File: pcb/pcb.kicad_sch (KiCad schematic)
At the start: 23 parts

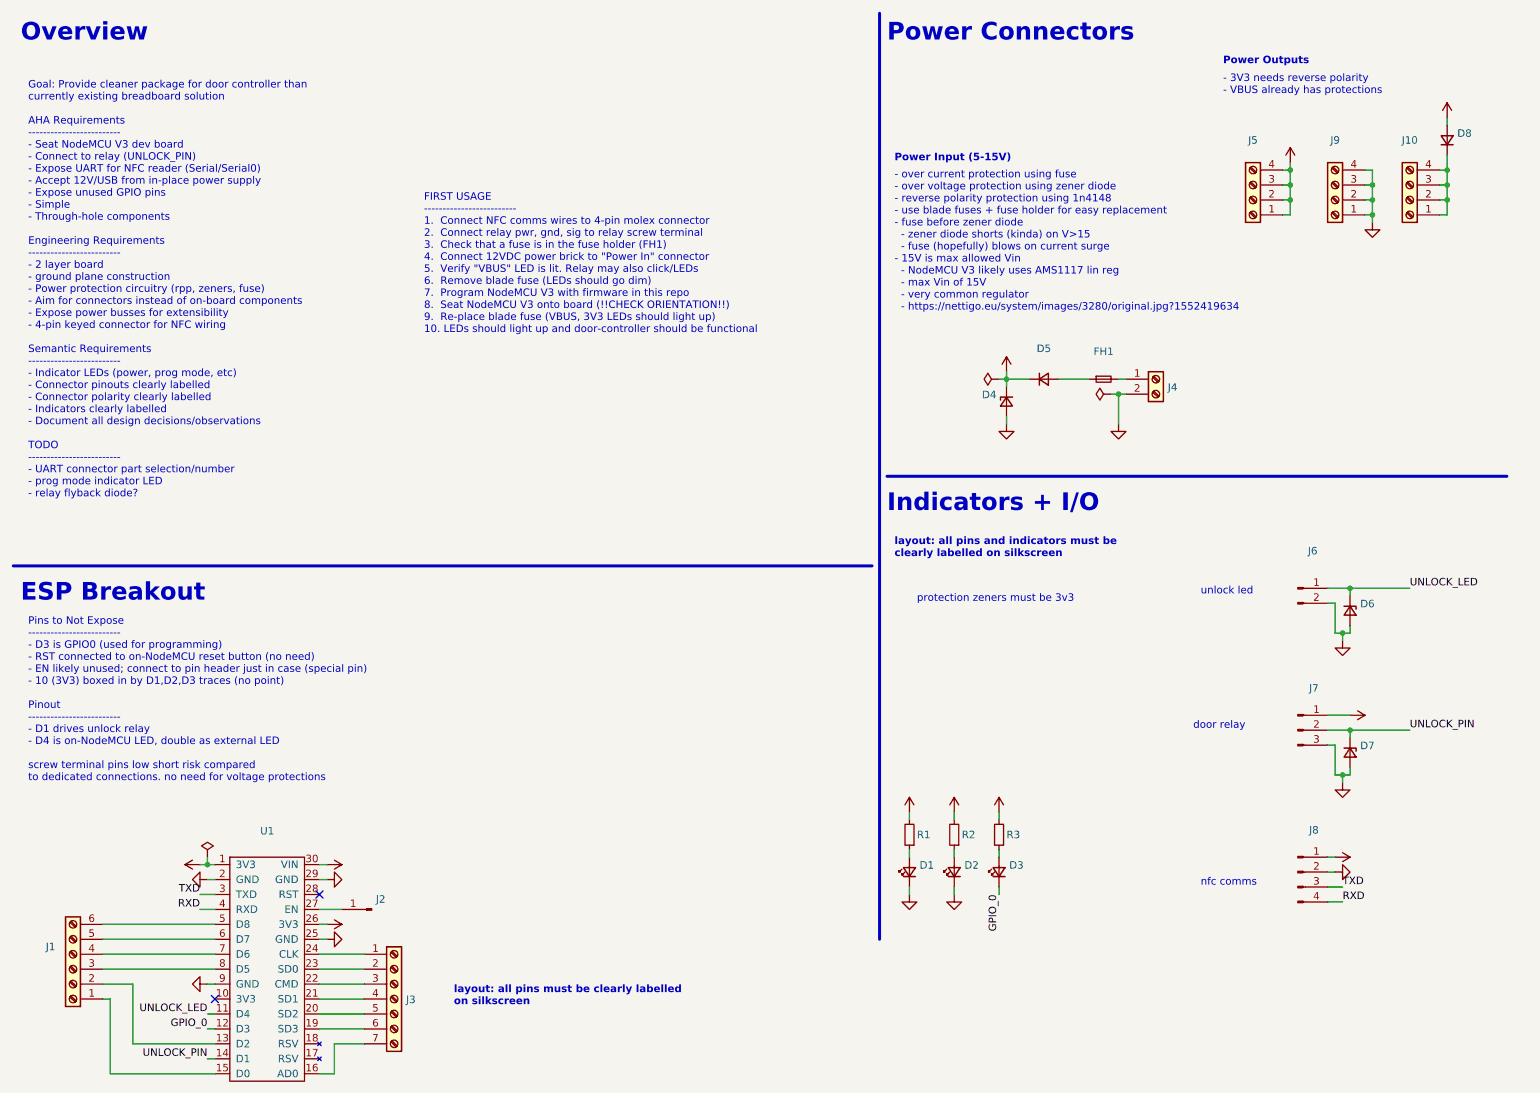
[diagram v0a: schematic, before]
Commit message: Update schematic with part numbers for BOM
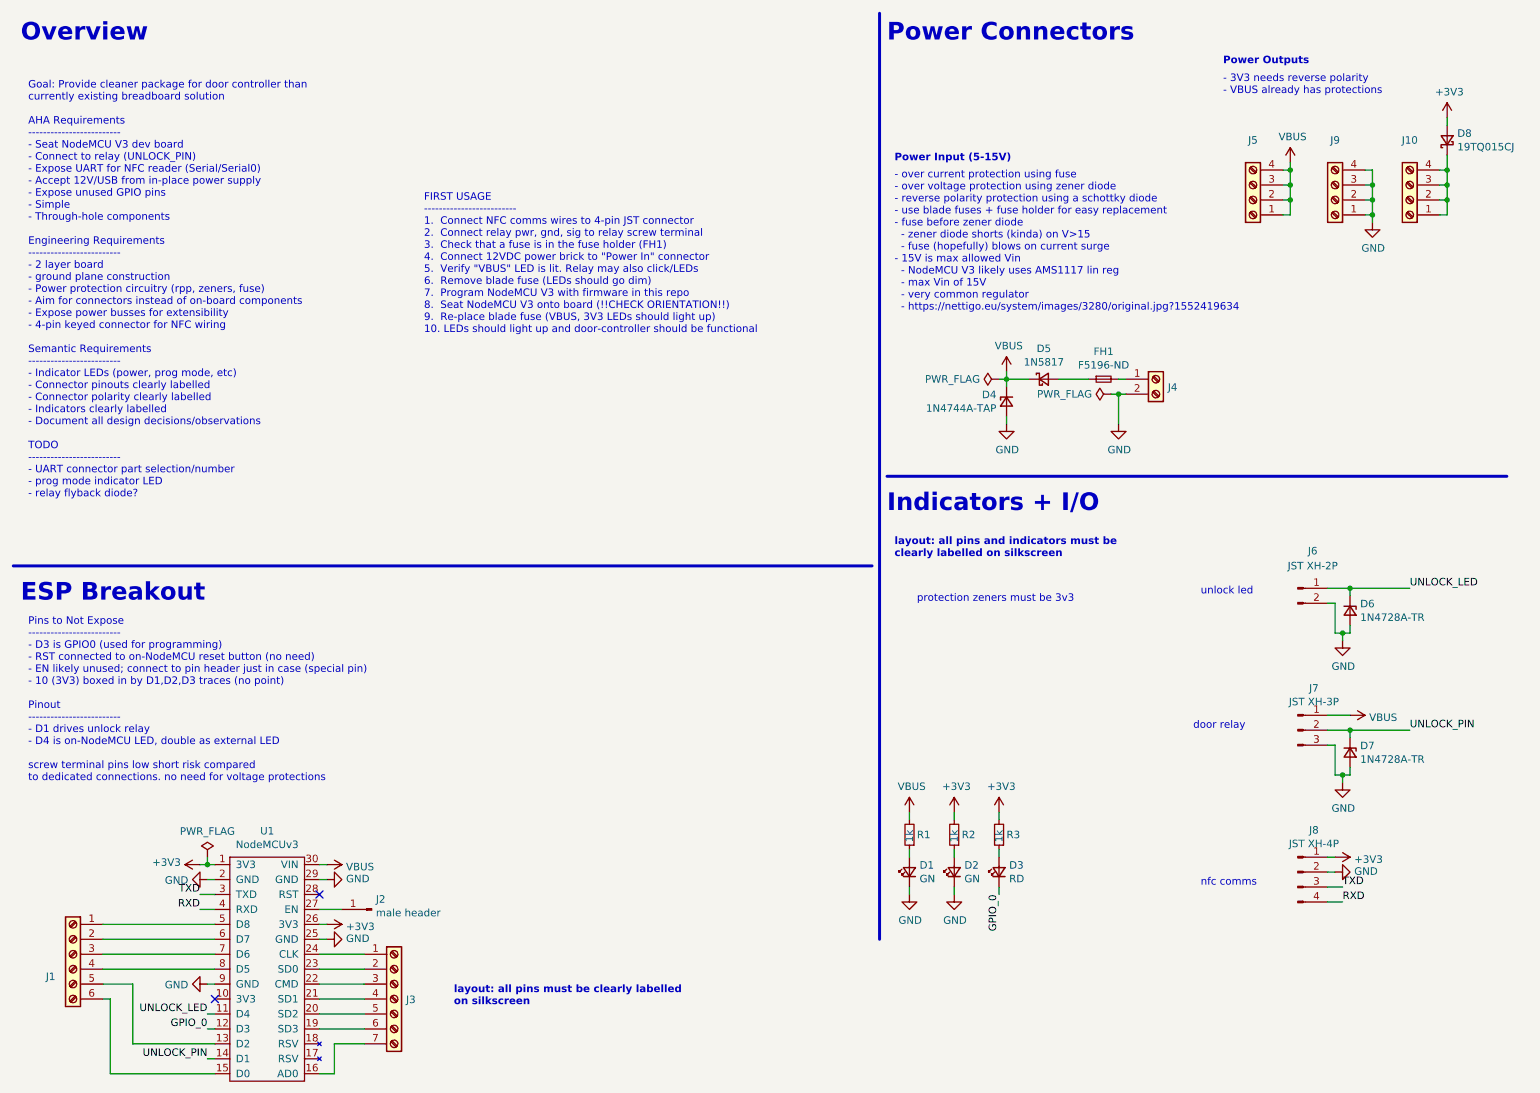
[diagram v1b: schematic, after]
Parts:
- D1, D2: value (none) -> GN; footprint (none) -> LED_THT:LED_D5.0mm; Digi-Key (none) -> 160-1130-ND; PartNo (none) -> LTL-4233
- D3: value (none) -> RD; footprint (none) -> LED_THT:LED_D5.0mm; Digi-Key (none) -> 160-1964-ND; PartNo (none) -> LTL-4263
- D4: value (none) -> 1N4744A-TAP; footprint (none) -> Diode_THT:D_DO-41_SOD81_P10.16mm_Horizontal; Digi-Key (none) -> 1N4744A-TAPGICT-ND; PartNo (none) -> 1N4744A-TAP
- D5: value (none) -> 1N5817; footprint (none) -> Diode_THT:D_DO-41_SOD81_P10.16mm_Horizontal; symbol Device:D_Small -> Device:D_Schottky_Small; Digi-Key (none) -> 1N5817-E3/54GICT-ND; PartNo (none) -> 1N5817-E3/54
- D6, D7: value (none) -> 1N4728A-TR; footprint (none) -> Diode_THT:D_DO-41_SOD81_P10.16mm_Horizontal; Digi-Key (none) -> 1N4728AVSCT-ND; PartNo (none) -> 1N4728A-TR
- D8: value (none) -> 19TQ015CJ; footprint (none) -> Package_TO_SOT_THT:TO-220-2_Vertical; symbol Device:D_Small -> Device:D_Schottky_Small; Digi-Key (none) -> 1655-1005-ND; PartNo (none) -> 19TQ015CJ
- FH1: value (none) -> F5196-ND; footprint (none) -> project:Blade Fuse Holder; Digi-Key (none) -> F5196-ND; PartNo (none) -> 178.6164.0002
- J1: value (none) -> Screw_Terminal_01x06; footprint (none) -> TerminalBlock_Phoenix:TerminalBlock_Phoenix_MPT-0,5-6-2.54_1x06_P2.54mm_Horizontal; Digi-Key (none) -> 277-1277-ND; PartNo (none) -> 1725698
- J10, J5, J9: value (none) -> Screw_Terminal_01x04; footprint (none) -> TerminalBlock_Phoenix:TerminalBlock_Phoenix_MPT-0,5-4-2.54_1x04_P2.54mm_Horizontal; Digi-Key (none) -> 277-1275-ND; PartNo (none) -> 1725672
- J2: value (none) -> male header; footprint (none) -> Connector_PinHeader_2.54mm:PinHeader_1x01_P2.54mm_Vertical; Digi-Key (none) -> 3M156413-01-ND; PartNo (none) -> 951101-8622-AR
- J3: value (none) -> Screw_Terminal_01x07; footprint (none) -> TerminalBlock_Phoenix:TerminalBlock_Phoenix_MPT-0,5-7-2.54_1x07_P2.54mm_Horizontal; Digi-Key (none) -> 277-1278-ND; PartNo (none) -> 1725708
- J4: value (none) -> Screw_Terminal_01x02; footprint (none) -> TerminalBlock_Phoenix:TerminalBlock_Phoenix_MPT-0,5-2-2.54_1x02_P2.54mm_Horizontal; Digi-Key (none) -> 277-1273-ND; PartNo (none) -> 1725656
- J6: value (none) -> JST XH-2P; footprint (none) -> Connector_JST:JST_XH_B2B-XH-AM_1x02_P2.50mm_Vertical; Digi-Key (none) -> 455-2946-ND; PartNo (none) -> B2B-XH-A-GU
- J7: value (none) -> JST XH-3P; footprint (none) -> Connector_JST:JST_XH_B3B-XH-AM_1x03_P2.50mm_Vertical; Digi-Key (none) -> 455-2231-ND; PartNo (none) -> B3B-XH-AM(LF)(SN)
- J8: value (none) -> JST XH-4P; footprint (none) -> Connector_JST:JST_XH_B4B-XH-AM_1x04_P2.50mm_Vertical; Digi-Key (none) -> 455-2237-ND; PartNo (none) -> B4B-XH-AM(LF)(SN)
- R1, R2, R3: value (none) -> 1k; footprint (none) -> Resistor_THT:R_Axial_DIN0207_L6.3mm_D2.5mm_P10.16mm_Horizontal; Digi-Key (none) -> CF14JT1K00CT-ND; PartNo (none) -> CF14JT1K00
- U1: value (none) -> NodeMCUv3; footprint (none) -> project:NodeMCUv3
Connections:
- net at U1.13 (D2): now also J1.5 (Pin_5); no longer J1.2 (Pin_2)
- net at U1.15 (D0): now also J1.6 (Pin_6); no longer J1.1 (Pin_1)
- net at U1.5 (D8): now also J1.1 (Pin_1); no longer J1.6 (Pin_6)
- net at U1.6 (D7): now also J1.2 (Pin_2); no longer J1.5 (Pin_5)
- net at U1.7 (D6): now also J1.3 (Pin_3); no longer J1.4 (Pin_4)
- net at U1.8 (D5): now also J1.4 (Pin_4); no longer J1.3 (Pin_3)
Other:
- note added: "- over current protection using fuse - over voltage protection using zener diode - reverse polarity protection using a schottky diode - use blade fuses + fuse holder for easy replacement - fuse before zener diode - zener diode shorts (kinda) on V>15 - fuse (hopefully) blows on current surge - 15V is max allowed Vin - NodeMCU V3 likely uses AMS1117 lin reg - max Vin of 15V - very common regulator 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"
- note added: "FIRST USAGE ------------------------- 1. Connect NFC comms wires to 4-pin JST connector 2. Connect relay pwr, gnd, sig to relay screw terminal 3. Check that a fuse is in the fuse holder (FH1) 4. Connect 12VDC power brick to "Power In" connector 5. Verify "VBUS" LED is lit. Relay may also click/LEDs 6. Remove blade fuse (LEDs should go dim) 7. Program NodeMCU V3 with firmware in this repo 8. Seat 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"
- note removed: "- over current protection using fuse - over voltage protection using zener diode - reverse polarity protection using 1n4148 - use blade fuses + fuse holder for easy replacement - fuse before zener diode - zener diode shorts (kinda) on V>15 - fuse (hopefully) blows on current surge - 15V is max allowed Vin - NodeMCU V3 likely uses AMS1117 lin reg - max Vin of 15V - very common regulator - https://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"
- note removed: "FIRST USAGE ------------------------- 1. Connect NFC comms wires to 4-pin molex connector 2. Connect relay pwr, gnd, sig to relay screw terminal 3. Check that a fuse is in the fuse holder (FH1) 4. Connect 12VDC power brick to "Power In" connector 5. Verify "VBUS" LED is lit. Relay may also click/LEDs 6. Remove blade fuse (LEDs should go dim) 7. Program NodeMCU V3 with firmware in this repo 8. Sea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"
- moved on the sheet: J1

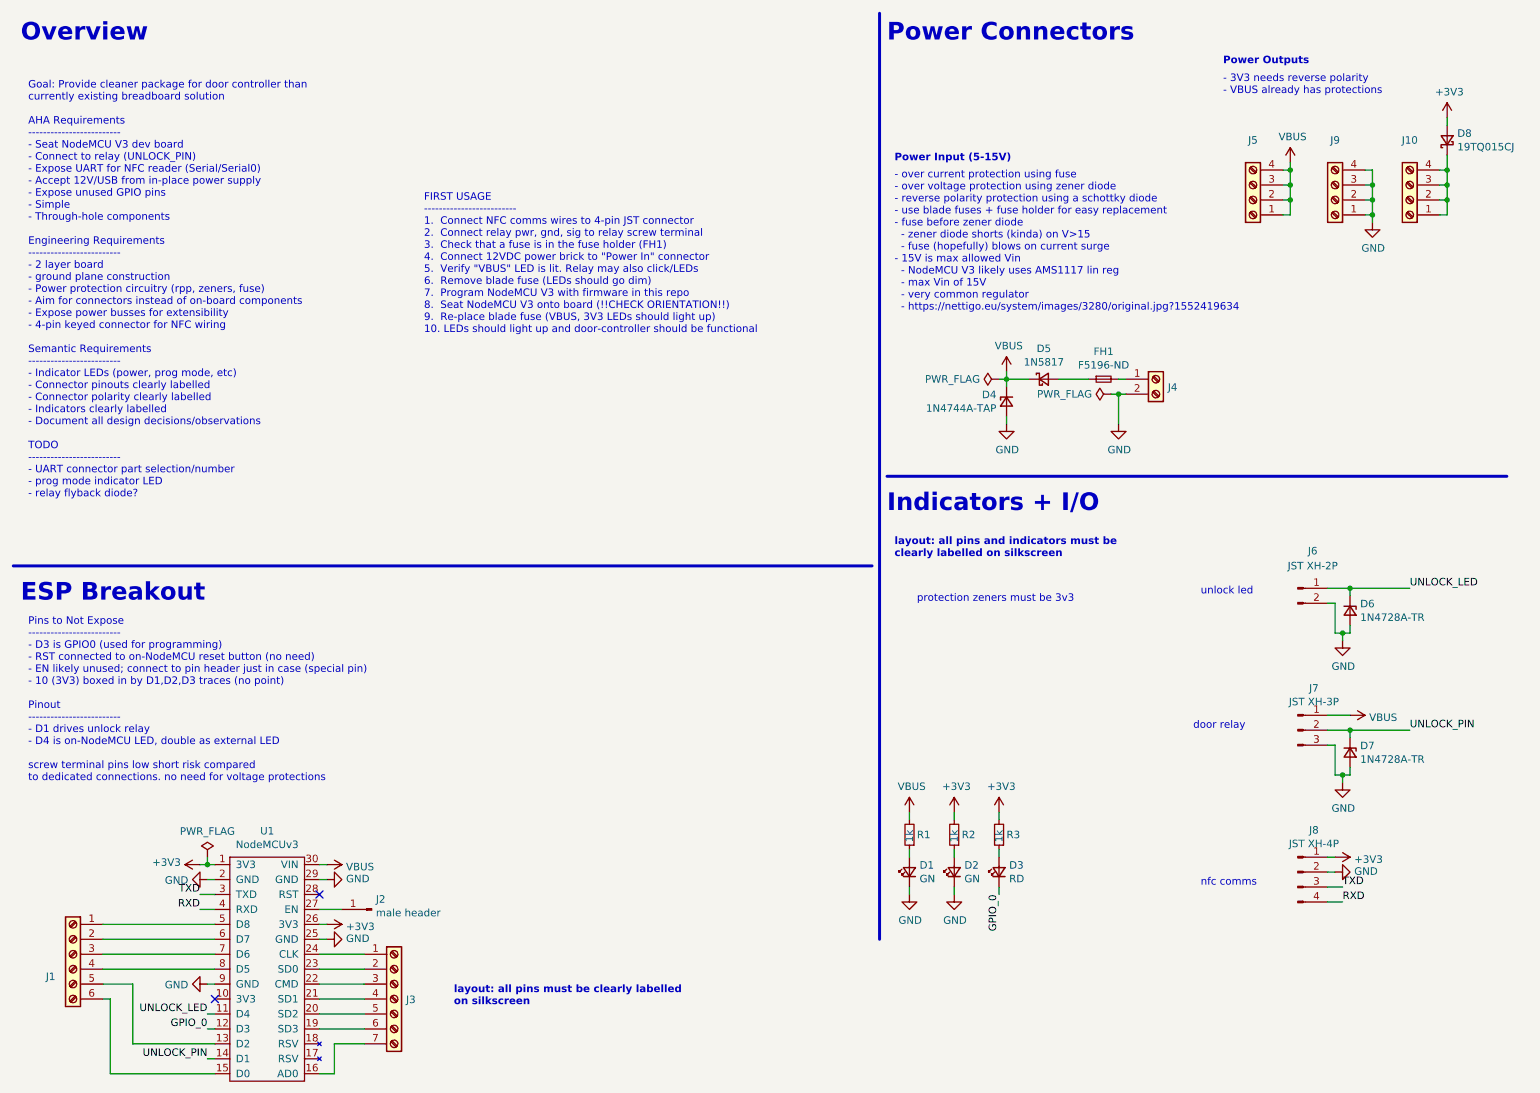
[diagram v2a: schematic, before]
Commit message: Added second relay and LED connectors to the PCB to allow controlling of two doors
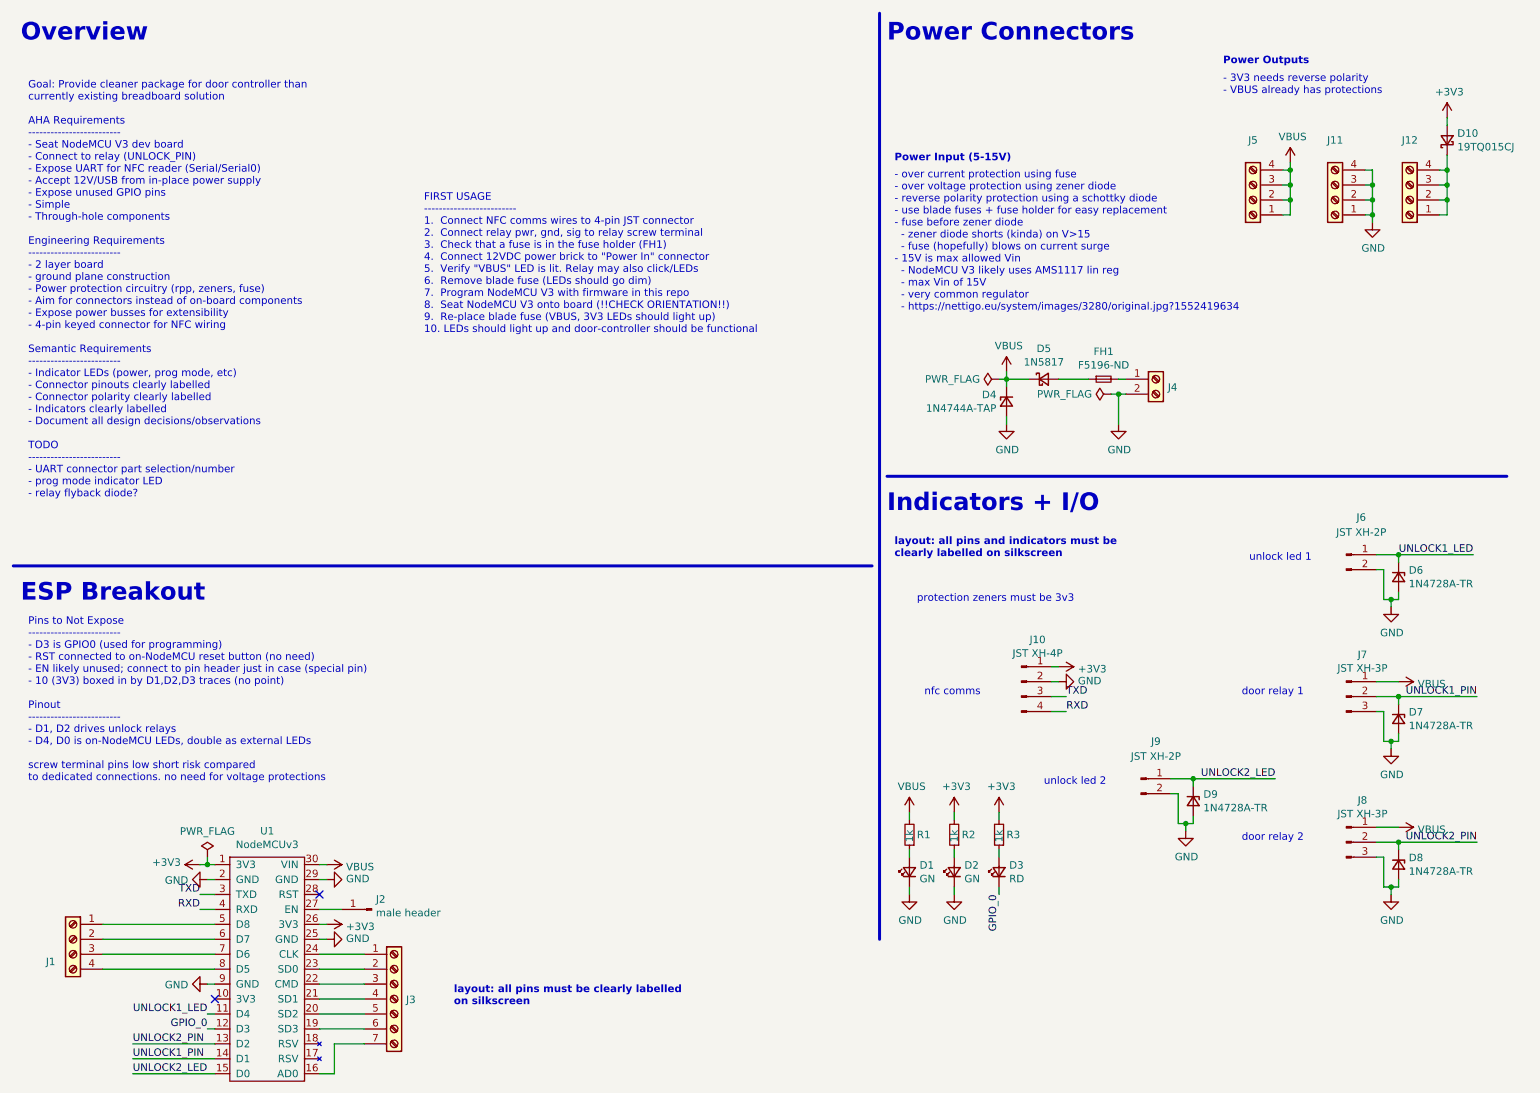
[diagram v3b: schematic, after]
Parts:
- added D8, D9: 1N4728A-TR, Diode_THT:D_DO-41_SOD81_P10.16mm_Horizontal, symbol Device:D_Zener_Small
- added J8: JST XH-3P, Connector_JST:JST_XH_B3B-XH-AM_1x03_P2.50mm_Vertical, symbol Connector:Conn_01x03_Male
- added J9: JST XH-2P, Connector_JST:JST_XH_B2B-XH-AM_1x02_P2.50mm_Vertical, symbol Connector:Conn_01x02_Male
- J1: footprint TerminalBlock_Phoenix:TerminalBlock_Phoenix_MPT-0,5-6-2.54_1x06_P2.54mm_Horizontal -> TerminalBlock_Phoenix:TerminalBlock_Phoenix_MPT-0,5-4-2.54_1x04_P2.54mm_Horizontal; symbol Connector:Screw_Terminal_01x06 -> Connector:Screw_Terminal_01x04; Digi-Key 277-1277-ND -> 277-1275-ND; PartNo 1725698 -> 1725672
- renumbered D8 to D10, J8 to J10, J9 to J11, J10 to J12
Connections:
- net GND: now also D8.2 (A), D9.2 (A), J8.3 (Pin_3), J9.2 (Pin_2)
- net VBUS: now also J8.1 (Pin_1)
- net UNLOCK2_PIN: now reaches U1.13 (D2)
- net UNLOCK2_PIN: now also D8.1 (K), J8.2 (Pin_2); no longer J1.5 (Pin_5)
- net UNLOCK2_LED: now reaches U1.15 (D0)
- net UNLOCK2_LED: now also D9.1 (K), J9.1 (Pin_1); no longer J1.6 (Pin_6)
- net UNLOCK_LED renamed UNLOCK1_LED
- net UNLOCK_PIN renamed UNLOCK1_PIN
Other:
- note added: "Pins to Not Expose ------------------------- - D3 is GPIO0 (used for programming) - RST connected to on-NodeMCU reset button (no need) - EN likely unused; connect to pin header just in case (special pin) - 10 (3V3) boxed in by D1,D2,D3 traces (no point) Pinout ------------------------- - D1, D2 drives unlock relays - D4, D0 is on-NodeMCU LEDs, double as external LEDs screw terminal pins low short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"
- note added: "door relay 1"
- note added: "door relay 2"
- note added: "unlock led 1"
- note added: "unlock led 2"
- note removed: "Pins to Not Expose ------------------------- - D3 is GPIO0 (used for programming) - RST connected to on-NodeMCU reset button (no need) - EN likely unused; connect to pin header just in case (special pin) - 10 (3V3) boxed in by D1,D2,D3 traces (no point) Pinout ------------------------- - D1 drives unlock relay - D4 is on-NodeMCU LED, double as external LED screw terminal pins low short risk compa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"
- note removed: "door relay"
- note removed: "unlock led"
- moved on the sheet: D6, D7, J10, J6, J7
